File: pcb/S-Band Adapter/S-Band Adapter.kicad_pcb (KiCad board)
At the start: 2 copper layers, 94 x 61 mm, 6 parts, among them J1 CT3151SP-2, J2 FTSH-107-01-L-DV-K-A, J3 ERF8-030-05.0-L-DV-TR, J4 532611071, J5 CT3151SP-2

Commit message: Improved docs
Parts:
- added G***: LOGO, LOGO, F.Cu at (171.7, 108.3)
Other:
- board text added: "Adapter"
- board text added: "Mystery Pins"
- board text added: "S-Band"
- board text added: "by Jannik"
- board text added: "w/ Backplane"
- board text added: "w/ ST-Link"

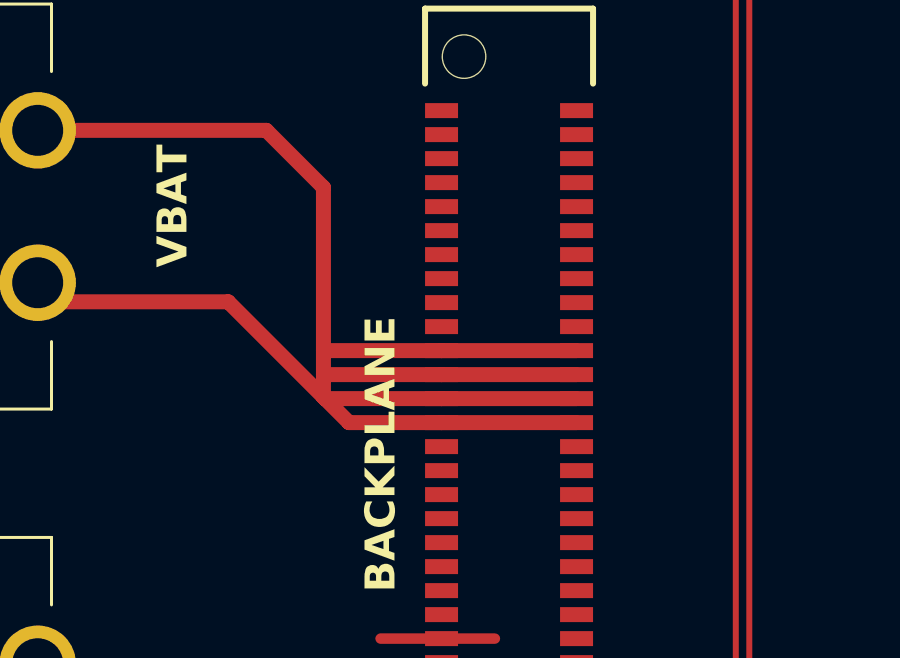
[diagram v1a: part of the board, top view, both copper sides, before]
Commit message: Fixed Pulling VSYS from BATPOS
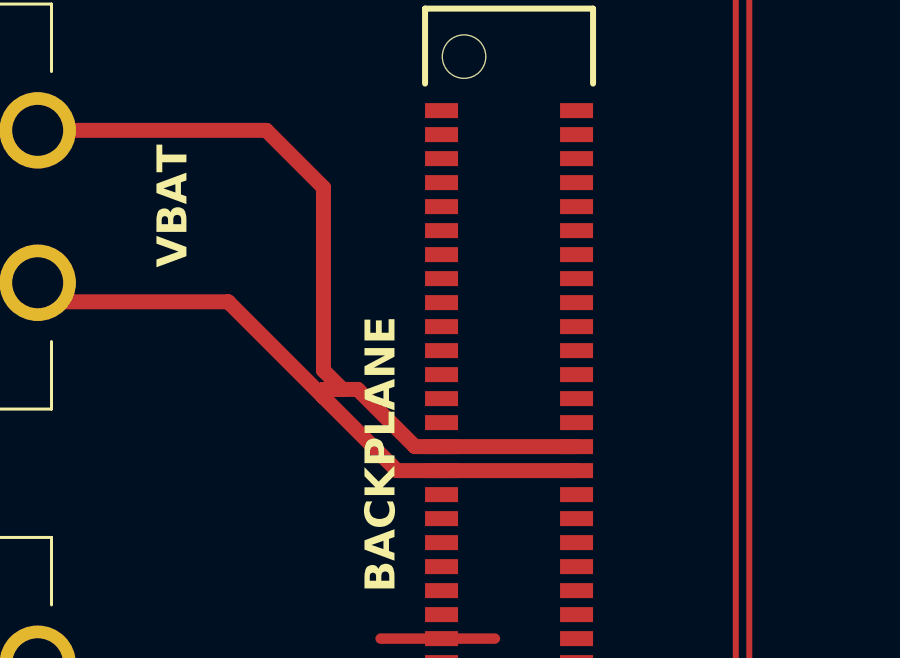
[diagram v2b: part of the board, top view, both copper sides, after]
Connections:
- J3 pad 29: unconnected-(J3-CH_VSYS-Pad29) -> VBUS
- J3 pad 30: unconnected-(J3-CH_VSYS-Pad30) -> VBUS
- J3 pad 31: unconnected-(J3-CH_VSYS-Pad31) -> VBUS
- J3 pad 32: unconnected-(J3-CH_VSYS-Pad32) -> VBUS
- J3 pad 33: VBUS -> unconnected-(J3-BATPOS-Pad33)
- J3 pad 34: VBUS -> unconnected-(J3-BATPOS-Pad34)
- J3 pad 35: VBUS -> unconnected-(J3-BATPOS-Pad35)
- J3 pad 36: VBUS -> unconnected-(J3-BATPOS-Pad36)
- J3 pad 37: VBUS -> unconnected-(J3-BATPOS-Pad37)
- J3 pad 38: VBUS -> unconnected-(J3-BATPOS-Pad38)
- J3 pad 39: VBUS -> unconnected-(J3-BATPOS-Pad39)
- J3 pad 40: VBUS -> unconnected-(J3-BATPOS-Pad40)
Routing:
- net VBUS: track 72.6 -> 58.1 mm
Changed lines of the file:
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@@
 	(net 16 "unconnected-(J3-1WUART-Pad15)")
 	(net 17 "unconnected-(J3-WATCHDOG-Pad13)")
-	(net 18 "unconnected-(J3-CH_VSYS-Pad29)")
-	(net 19 "unconnected-(J3-CH_VSYS-Pad30)")
+	(net 18 "unconnected-(J3-BATPOS-Pad40)")
+	(net 19 "unconnected-(J3-BATPOS-Pad36)")
 	(net 20 "unconnected-(J3-CH_3V3-Pad23)")
 	(net 21 "unconnected-(J3-CH_3V3-Pad21)")
@@
 	(net 24 "unconnected-(J3-SCL_Ext_2-Pad10)")
 	(net 25 "unconnected-(J3-CH_5V-Pad28)")
-	(net 26 "unconnected-(J3-CH_VSYS-Pad31)")
+	(net 26 "unconnected-(J3-BATPOS-Pad35)")
 	(net 27 "unconnected-(J3-CH_3V3-Pad22)")
 	(net 28 "unconnected-(J3-3V3_Init-Pad59)")
 	(net 29 "unconnected-(J3-CH_5V-Pad25)")
 	(net 30 "unconnected-(J3-SDA_Ext_1-Pad02)")
-	(net 31 "unconnected-(J3-CH_VSYS-Pad32)")
+	(net 31 "unconnected-(J3-BATPOS-Pad37)")
 	(net 32 "unconnected-(J3-SDA_Ext_2-Pad08)")
 	(net 33 "unconnected-(J3-NC3-Pad20)")
@@
 	(net 133 "/UART_N")
 	(net 134 "/UART_P")
+	(net 135 "unconnected-(J3-BATPOS-Pad39)")
+	(net 136 "unconnected-(J3-BATPOS-Pad34)")
+	(net 137 "unconnected-(J3-BATPOS-Pad33)")
+	(net 138 "unconnected-(J3-BATPOS-Pad38)")
 	(footprint "KiCad:CT3151SP2"
 		(layer "F.Cu")
@@
 			(size 0.5 1.1)
 			(layers "F.Cu" "F.Mask" "F.Paste")
-			(net 18 "unconnected-(J3-CH_VSYS-Pad29)")
+			(net 13 "VBUS")
 			(pinfunction "CH_VSYS")
-			(pintype "passive+no_connect")
+			(pintype "passive")
 			(solder_mask_margin 0.102)
 		)
@@
 			(size 0.5 1.1)
 			(layers "F.Cu" "F.Mask" "F.Paste")
-			(net 19 "unconnected-(J3-CH_VSYS-Pad30)")
+			(net 13 "VBUS")
 			(pinfunction "CH_VSYS")
-			(pintype "passive+no_connect")
+			(pintype "passive")
 			(solder_mask_margin 0.102)
 		)
@@
 			(size 0.5 1.1)
 			(layers "F.Cu" "F.Mask" "F.Paste")
-			(net 26 "unconnected-(J3-CH_VSYS-Pad31)")
+			(net 13 "VBUS")
 			(pinfunction "CH_VSYS")
-			(pintype "passive+no_connect")
+			(pintype "passive")
 			(solder_mask_margin 0.102)
 		)
@@
 			(size 0.5 1.1)
 			(layers "F.Cu" "F.Mask" "F.Paste")
-			(net 31 "unconnected-(J3-CH_VSYS-Pad32)")
+			(net 13 "VBUS")
 			(pinfunction "CH_VSYS")
-			(pintype "passive+no_connect")
+			(pintype "passive")
 			(solder_mask_margin 0.102)
 		)
@@
 			(size 0.5 1.1)
 			(layers "F.Cu" "F.Mask" "F.Paste")
-			(net 13 "VBUS")
+			(net 137 "unconnected-(J3-BATPOS-Pad33)")
 			(pinfunction "BATPOS")
-			(pintype "passive")
+			(pintype "passive+no_connect")
 			(solder_mask_margin 0.102)
 		)
@@
 			(size 0.5 1.1)
 			(layers "F.Cu" "F.Mask" "F.Paste")
-			(net 13 "VBUS")
+			(net 136 "unconnected-(J3-BATPOS-Pad34)")
 			(pinfunction "BATPOS")
-			(pintype "passive")
+			(pintype "passive+no_connect")
 			(solder_mask_margin 0.102)
 		)
@@
 			(size 0.5 1.1)
 			(layers "F.Cu" "F.Mask" "F.Paste")
-			(net 13 "VBUS")
+			(net 26 "unconnected-(J3-BATPOS-Pad35)")
 			(pinfunction "BATPOS")
-			(pintype "passive")
+			(pintype "passive+no_connect")
 			(solder_mask_margin 0.102)
 		)
@@
 			(size 0.5 1.1)
 			(layers "F.Cu" "F.Mask" "F.Paste")
-			(net 13 "VBUS")
+			(net 19 "unconnected-(J3-BATPOS-Pad36)")
 			(pinfunction "BATPOS")
-			(pintype "passive")
+			(pintype "passive+no_connect")
 			(solder_mask_margin 0.102)
 		)
@@
 			(size 0.5 1.1)
 			(layers "F.Cu" "F.Mask" "F.Paste")
-			(net 13 "VBUS")
+			(net 31 "unconnected-(J3-BATPOS-Pad37)")
 			(pinfunction "BATPOS")
-			(pintype "passive")
+			(pintype "passive+no_connect")
 			(solder_mask_margin 0.102)
 		)
@@
 			(size 0.5 1.1)
 			(layers "F.Cu" "F.Mask" "F.Paste")
-			(net 13 "VBUS")
+			(net 138 "unconnected-(J3-BATPOS-Pad38)")
 			(pinfunction "BATPOS")
-			(pintype "passive")
+			(pintype "passive+no_connect")
 			(solder_mask_margin 0.102)
 		)
@@
 			(size 0.5 1.1)
 			(layers "F.Cu" "F.Mask" "F.Paste")
-			(net 13 "VBUS")
+			(net 135 "unconnected-(J3-BATPOS-Pad39)")
 			(pinfunction "BATPOS")
-			(pintype "passive")
+			(pintype "passive+no_connect")
 			(solder_mask_margin 0.102)
 		)
@@
 			(size 0.5 1.1)
 			(layers "F.Cu" "F.Mask" "F.Paste")
-			(net 13 "VBUS")
+			(net 18 "unconnected-(J3-BATPOS-Pad40)")
 			(pinfunction "BATPOS")
-			(pintype "passive")
+			(pintype "passive+no_connect")
 			(solder_mask_margin 0.102)
 		)
@@
 	)
 	(segment
-		(start 169.05 84.685)
-		(end 163.335 84.685)
-		(width 0.5)
-		(layer "F.Cu")
-		(net 13)
-	)
-	(segment
-		(start 176.162 87.912)
-		(end 180.662 87.912)
+		(start 174.677 90.312)
+		(end 176.162 90.312)
 		(width 0.5)
 		(layer "F.Cu")
@@
 	)
 	(segment
-		(start 176.162 88.712)
-		(end 173.077 88.712)
+		(start 172.225 87.606)
+		(end 172.86 87.606)
 		(width 0.5)
 		(layer "F.Cu")
@@
 	)
 	(segment
-		(start 172.277 87.912)
-		(end 172.225 87.86)
+		(start 169.05 84.685)
+		(end 163.335 84.685)
 		(width 0.5)
 		(layer "F.Cu")
@@
 	)
 	(segment
-		(start 172.225 87.112)
-		(end 176.162 87.112)
+		(start 172.225 87.86)
+		(end 174.677 90.312)
 		(width 0.5)
 		(layer "F.Cu")
@@
 	)
 	(segment
-		(start 163.335 84.685)
-		(end 162.7 84.05)
+		(start 176.162 90.312)
+		(end 180.662 90.312)
 		(width 0.5)
 		(layer "F.Cu")
@@
 	)
 	(segment
-		(start 176.162 86.312)
-		(end 172.225 86.312)
+		(start 173.368 87.606)
+		(end 175.274 89.512)
 		(width 0.5)
 		(layer "F.Cu")
@@
 	)
 	(segment
-		(start 176.162 87.112)
-		(end 180.662 87.112)
+		(start 163.335 84.685)
+		(end 162.7 84.05)
 		(width 0.5)
 		(layer "F.Cu")
@@
 	)
 	(segment
-		(start 176.162 87.912)
-		(end 172.277 87.912)
+		(start 172.225 87.606)
+		(end 173.368 87.606)
 		(width 0.5)
 		(layer "F.Cu")
@@
 	)
 	(segment
-		(start 157.62 84.05)
-		(end 162.7 84.05)
+		(start 172.225 80.875)
+		(end 170.32 78.97)
 		(width 0.5)
 		(layer "F.Cu")
@@
 	)
 	(segment
-		(start 172.225 87.112)
-		(end 172.225 86.312)
+		(start 172.86 87.606)
+		(end 172.225 86.971)
 		(width 0.5)
 		(layer "F.Cu")
@@
 	)
 	(segment
-		(start 176.162 88.712)
-		(end 180.662 88.712)
+		(start 172.225 86.971)
+		(end 172.225 80.875)
 		(width 0.5)
 		(layer "F.Cu")
@@
 	)
 	(segment
-		(start 176.162 86.312)
-		(end 180.662 86.312)
+		(start 157.62 84.05)
+		(end 162.7 84.05)
 		(width 0.5)
 		(layer "F.Cu")
@@
 	(segment
 		(start 172.225 87.86)
-		(end 169.05 84.685)
+		(end 172.225 87.606)
 		(width 0.5)
 		(layer "F.Cu")
@@
 	)
 	(segment
-		(start 173.077 88.712)
-		(end 172.277 87.912)
+		(start 175.274 89.512)
+		(end 176.162 89.512)
 		(width 0.5)
 		(layer "F.Cu")
@@
 	(segment
 		(start 172.225 87.86)
-		(end 172.225 87.112)
-		(width 0.5)
-		(layer "F.Cu")
-		(net 13)
-	)
-	(segment
-		(start 172.225 80.875)
-		(end 170.32 78.97)
+		(end 169.05 84.685)
 		(width 0.5)
 		(layer "F.Cu")
@@
 	)
 	(segment
-		(start 172.225 86.312)
-		(end 172.225 80.875)
+		(start 176.162 89.512)
+		(end 180.662 89.512)
 		(width 0.5)
 		(layer "F.Cu")

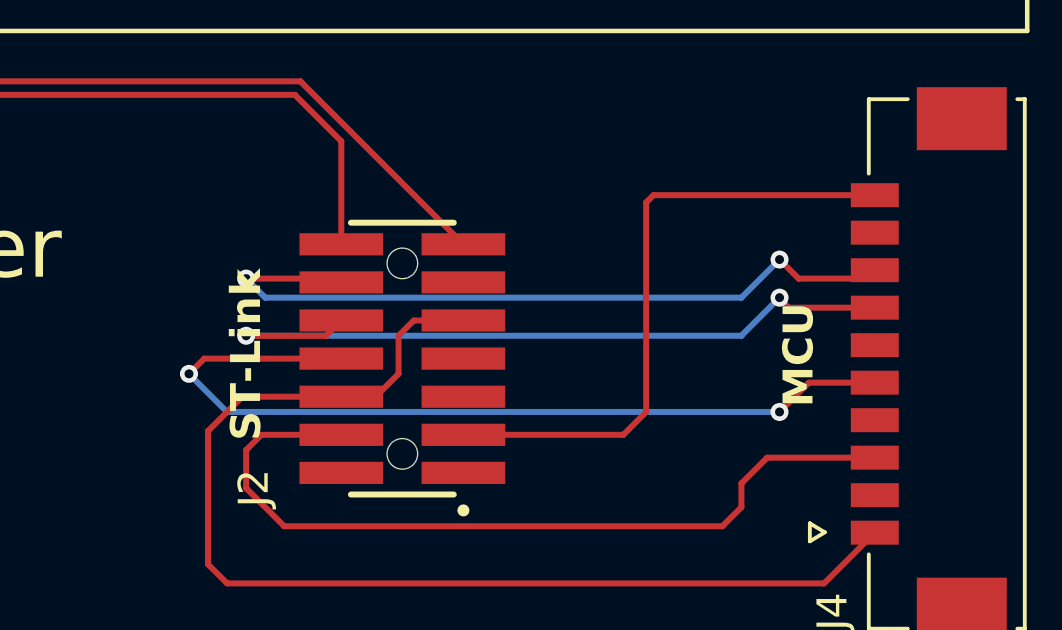
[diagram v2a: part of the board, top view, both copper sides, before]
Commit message: Improved 3.3V net track width
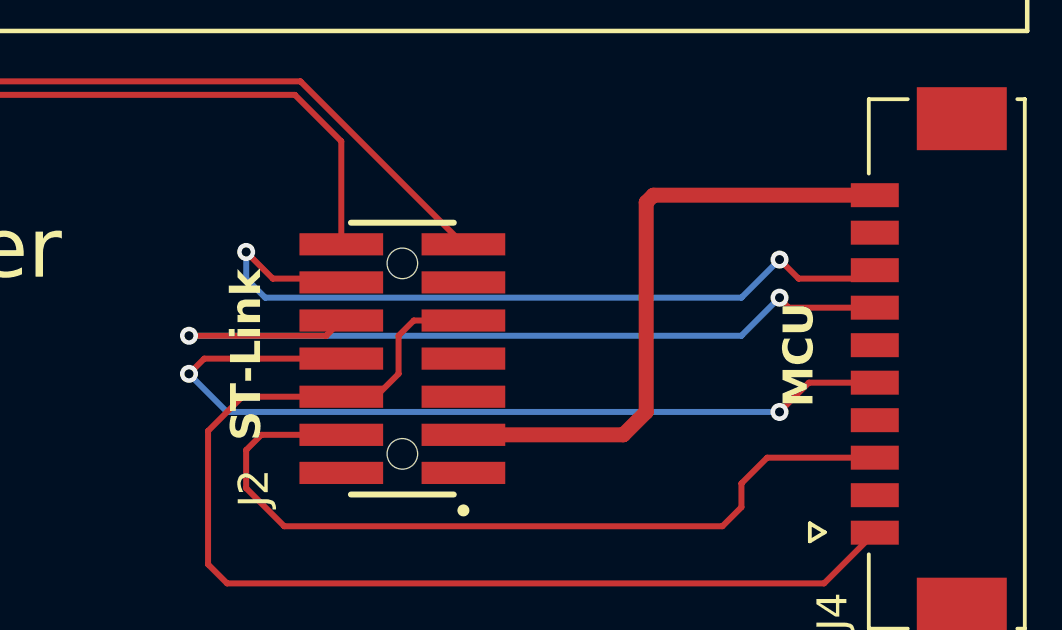
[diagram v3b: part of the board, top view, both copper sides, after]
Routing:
- net /JTAG_DI: track 25.0 -> 28.8 mm
- net /JTAG_NRST: track 25.3 -> 26.6 mm
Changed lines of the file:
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@@
 	)
 	(segment
-		(start 223.657 81.002)
-		(end 223.53 80.875)
+		(start 223.53 80.875)
+		(end 223.657 81.002)
+		(width 0.2)
+		(layer "F.Cu")
+		(net 3)
+	)
+	(segment
+		(start 220.485 79.986)
+		(end 221.374 80.875)
 		(width 0.2)
 		(layer "F.Cu")
@@
 	)
 	(segment
-		(start 223.53 80.875)
-		(end 220.485 80.875)
+		(start 221.374 80.875)
+		(end 223.53 80.875)
 		(width 0.2)
 		(layer "F.Cu")
@@
 	)
 	(via
-		(at 220.485 80.875)
+		(at 220.485 79.986)
 		(size 0.6)
 		(drill 0.3)
@@
 	)
 	(segment
+		(start 221.12 81.51)
+		(end 236.995 81.51)
+		(width 0.2)
+		(layer "B.Cu")
+		(net 3)
+	)
+	(segment
+		(start 220.485 80.875)
+		(end 221.12 81.51)
+		(width 0.2)
+		(layer "B.Cu")
+		(net 3)
+	)
+	(segment
+		(start 220.485 79.986)
+		(end 220.485 80.875)
+		(width 0.2)
+		(layer "B.Cu")
+		(net 3)
+	)
+	(segment
 		(start 236.995 81.51)
-		(end 221.12 81.51)
-		(width 0.2)
-		(layer "B.Cu")
-		(net 3)
-	)
-	(segment
-		(start 221.12 81.51)
-		(end 220.485 80.875)
-		(width 0.2)
-		(layer "B.Cu")
-		(net 3)
-	)
-	(segment
-		(start 238.265 80.24)
-		(end 236.995 81.51)
+		(end 238.265 80.24)
 		(width 0.2)
 		(layer "B.Cu")
@@
 	)
 	(segment
+		(start 238.265 81.51)
+		(end 238.265 81.543)
+		(width 0.2)
+		(layer "F.Cu")
+		(net 6)
+	)
+	(segment
+		(start 223.149 82.78)
+		(end 223.657 82.272)
+		(width 0.2)
+		(layer "F.Cu")
+		(net 6)
+	)
+	(segment
 		(start 238.566 81.844)
 		(end 241.44 81.844)
@@
 	)
 	(segment
-		(start 223.149 82.78)
-		(end 223.657 82.272)
-		(width 0.2)
-		(layer "F.Cu")
-		(net 6)
-	)
-	(segment
-		(start 238.265 81.51)
-		(end 238.265 81.543)
-		(width 0.2)
-		(layer "F.Cu")
-		(net 6)
-	)
-	(segment
-		(start 220.485 82.78)
+		(start 218.58 82.78)
 		(end 223.149 82.78)
 		(width 0.2)
@@
 	)
 	(via
-		(at 220.485 82.78)
+		(at 218.58 82.78)
 		(size 0.6)
 		(drill 0.3)
@@
 	(segment
 		(start 236.995 82.78)
-		(end 220.485 82.78)
+		(end 218.58 82.78)
 		(width 0.2)
 		(layer "B.Cu")
@@
 		(start 233.82 85.32)
 		(end 233.058 86.082)
-		(width 0.2)
+		(width 0.5)
 		(layer "F.Cu")
 		(net 9)
@@
 		(start 233.058 86.082)
 		(end 227.727 86.082)
-		(width 0.2)
+		(width 0.5)
 		(layer "F.Cu")
 		(net 9)
@@
 		(start 234.061 78.094)
 		(end 233.82 78.335)
-		(width 0.2)
+		(width 0.5)
 		(layer "F.Cu")
 		(net 9)
@@
 		(start 241.44 78.094)
 		(end 234.061 78.094)
-		(width 0.2)
+		(width 0.5)
 		(layer "F.Cu")
 		(net 9)
@@
 		(start 233.82 78.335)
 		(end 233.82 85.32)
-		(width 0.2)
-		(layer "F.Cu")
-		(net 9)
+		(width 0.5)
+		(layer "F.Cu")
+		(net 9)

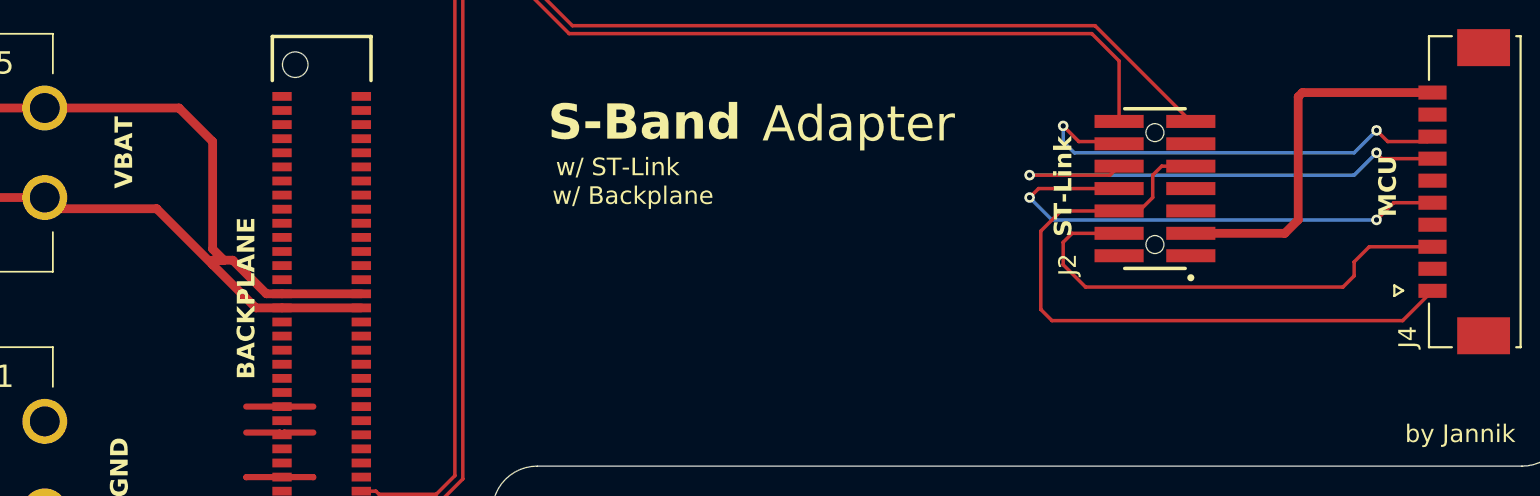
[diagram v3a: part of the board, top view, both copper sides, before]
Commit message: Added Debug_Reset button & fixed VBAT label
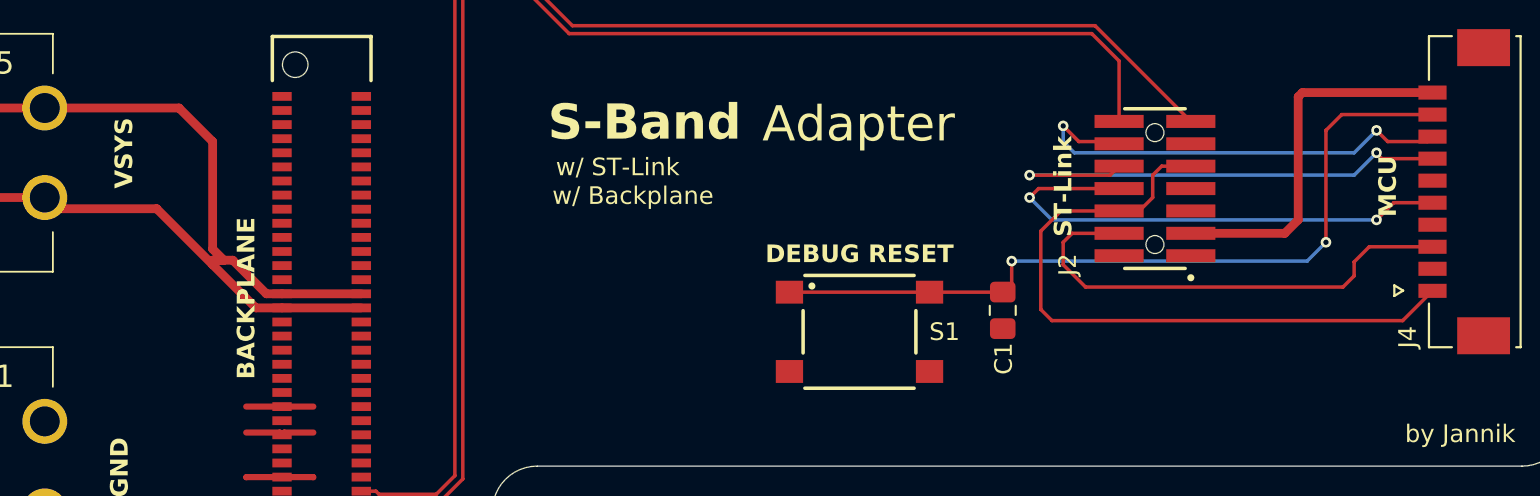
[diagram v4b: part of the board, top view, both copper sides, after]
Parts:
- added C1: 100nF, Capacitor_SMD:C_0805_2012Metric_Pad1.18x1.45mm_HandSolder, F.Cu at (217.1, 90.5)
- added S1: 430152050826, 430152050826:430152050826, F.Cu at (208.9, 91.7)
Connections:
- J4 pad 9: unconnected-(J4-Debug_reset-Pad9) -> /DEBUG_Reset
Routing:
- net /DEBUG_Reset: track 0.00 -> 45.1 mm, vias 0 -> 2
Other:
- board text added: "DEBUG RESET"
- board text added: "VSYS"
- board text removed: "VBAT"
